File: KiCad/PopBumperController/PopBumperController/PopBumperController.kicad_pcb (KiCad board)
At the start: 2 copper layers, 132.5 x 83 mm, 63 parts, among them J1 Conn_01x02, J10 Conn_01x03, J11 Conn_01x03, J12 Conn_01x02, J13 Conn_01x03, J14 Conn_01x02, J15 Conn_01x03, J16 Conn_01x03, J2 Conn_01x03, J3 Conn_01x02, J4 Conn_01x02, J6 Conn_01x02, J7 Conn_01x02, J8 Conn_01x02, J9 Conn_01x03, Q1 TIP102, Q10 2N3904, Q11 TIP102, Q12 TIP102, Q13 2N3904, Q14 2N3904, Q16 TIP102, Q17 TIP102, Q2 TIP102, Q3 TIP102, Q4 2N3904, Q5 2N3904, Q6 2N3904, Q7 TIP102, Q8 TIP102, Q9 2N3904, U1 Pico

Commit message: Fix schematic issues, start PCB layout
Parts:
- removed the ? at (29.5, 115.5)
- removed the ? at (29.5, 42.5)
- removed J10, J11, J9: Conn_01x03, Connector_PinHeader_2.54mm:PinHeader_1x03_P2.54mm_Vertical
- removed J12, J14, J8, LED1, LED2, LED3, SOL1, SOL2, SOL3, SOL4, SOL5, SOL8, SOL9, SOL_L1, SOL_R1: Conn_01x02, Connector_JST:JST_XH_B2B-XH-A_1x02_P2.50mm_Vertical
- removed J13, J15, J16, SEN1, SEN2, SEN3, Vin1: Conn_01x03, Connector_JST:JST_XH_B3B-XH-A_1x03_P2.50mm_Vertical
- removed REF**: MountingHole_3.2mm_M3_ISO14580_Pad, MountingHole:MountingHole_3.2mm_M3_ISO14580_Pad
- added C1: 100 uF, Capacitor_THT:CP_Radial_D8.0mm_P3.50mm, F.Cu at (147.3, 152.4)
- added C10: 1000 uF, Capacitor_THT:CP_Radial_D10.0mm_P5.00mm, F.Cu at (268.3, 28.8)
- added C11: 100 uF, Capacitor_THT:CP_Radial_D8.0mm_P3.50mm, F.Cu at (323.0, 3.20)
- added C12: 15000 uF, Capacitor_THT:CP_Radial_D25.0mm_P10.00mm_SnapIn, F.Cu at (182.9, -18.3)
- added C2: 1000 uF, Capacitor_THT:CP_Radial_D10.0mm_P5.00mm, F.Cu at (300.0, 4.20)
- added C3: 1000 uF, Capacitor_THT:CP_Radial_D10.0mm_P5.00mm, F.Cu at (252.1, 54.1)
- added C4: 1000 uF, Capacitor_THT:CP_Radial_D10.0mm_P5.00mm, F.Cu at (253.0, 41.4)
- added C5: 1000 uF, Capacitor_THT:CP_Radial_D10.0mm_P5.00mm, F.Cu at (240.1, 61.9)
- added C6: 1000 uF, Capacitor_THT:CP_Radial_D10.0mm_P5.00mm, F.Cu at (282.2, 23.6)
- added C7: 1000 uF, Capacitor_THT:CP_Radial_D10.0mm_P5.00mm, F.Cu at (298.5, 15.8)
- added C8: 1000 uF, Capacitor_THT:CP_Radial_D10.0mm_P5.00mm, F.Cu at (286.7, 12.0)
- added C9: 1000 uF, Capacitor_THT:CP_Radial_D10.0mm_P5.00mm, F.Cu at (136.1, 43.2)
- added DT_SERVO1: 2.54mm, Connector_PinHeader_2.54mm:PinHeader_1x03_P2.54mm_Vertical, F.Cu at (106.7, 111.7)
- added DT_SERVO2: 2.54mm, Connector_PinHeader_2.54mm:PinHeader_1x03_P2.54mm_Vertical, F.Cu at (111.8, 111.7)
- added DT_SERVO3: 2.54mm, Connector_PinHeader_2.54mm:PinHeader_1x03_P2.54mm_Vertical, F.Cu at (116.8, 111.7)
- added DT_SW1: JST-XH x2, Connector_JST:JST_XH_B2B-XH-A_1x02_P2.50mm_Vertical, F.Cu at (110.5, 118.1)
- added DT_SW2: JST-XH x2, Connector_JST:JST_XH_B2B-XH-A_1x02_P2.50mm_Vertical, F.Cu at (110.5, 127.0)
- added DT_SW3: JST-XH x2, Connector_JST:JST_XH_B2B-XH-A_1x02_P2.50mm_Vertical, F.Cu at (110.5, 135.9)
- added J5: HYP_SIG, Connector_JST:JST_XH_B3B-XH-A_1x03_P2.50mm_Vertical, F.Cu at (105.5, 99.1)
- added L1: 47 mH, Inductor_THT:L_Radial_D12.0mm_P5.00mm_Fastron_11P, F.Cu at (135.9, 149.9)
- added LED_PB1: + -, Connector_JST:JST_XH_B2B-XH-A_1x02_P2.50mm_Vertical, F.Cu at (330.9, 11.3)
- added LED_PB2: + -, Connector_JST:JST_XH_B2B-XH-A_1x02_P2.50mm_Vertical, F.Cu at (292.8, 40.6)
- added LED_PB3: + -, Connector_JST:JST_XH_B2B-XH-A_1x02_P2.50mm_Vertical, F.Cu at (298.6, 32.7)
- added LED_SLL1: + -, Connector_JST:JST_XH_B2B-XH-A_1x02_P2.50mm_Vertical, F.Cu at (333.0, 1.80)
- added LED_SLR1: + -, Connector_JST:JST_XH_B2B-XH-A_1x02_P2.50mm_Vertical, F.Cu at (321.5, 11.3)
- added PB_SENS1: JST-XH x3, Connector_JST:JST_XH_B3B-XH-A_1x03_P2.50mm_Vertical, F.Cu at (288.0, 1.80)
- added PB_SENS2: JST-XH x3, Connector_JST:JST_XH_B3B-XH-A_1x03_P2.50mm_Vertical, F.Cu at (270.2, 18.6)
- added PB_SENS3: JST-XH x3, Connector_JST:JST_XH_B3B-XH-A_1x03_P2.50mm_Vertical, F.Cu at (240.1, 51.7)
- added Q15: 2N3904, Package_TO_SOT_THT:TO-92_Inline, F.Cu at (302.3, 48.2)
- added Q18: TIP102, Package_TO_SOT_THT:TO-220-3_Vertical, F.Cu at (311.5, 2.35)
- added Q19: 2N3904, Package_TO_SOT_THT:TO-92_Inline, F.Cu at (163.8, 31.8)
- added Q20: 2N3904, Package_TO_SOT_THT:TO-92_Inline, F.Cu at (306.6, 32.6)
- added Q21: TIP102, Package_TO_SOT_THT:TO-220-3_Vertical, F.Cu at (146.1, 33.2)
- added Q22: TIP102, Package_TO_SOT_THT:TO-220-3_Vertical, F.Cu at (293.7, 25.4)
- added R1: 330, Resistor_THT:R_Axial_DIN0309_L9.0mm_D3.2mm_P12.70mm_Horizontal, F.Cu at (240.5, 0.80)
- added R10: 470k, Resistor_THT:R_Axial_DIN0309_L9.0mm_D3.2mm_P12.70mm_Horizontal, F.Cu at (198.1, -16.5)
- added R11: 470k, Resistor_THT:R_Axial_DIN0309_L9.0mm_D3.2mm_P12.70mm_Horizontal, F.Cu at (147.3, 143.5)
- added R2: 330, Resistor_THT:R_Axial_DIN0309_L9.0mm_D3.2mm_P12.70mm_Horizontal, F.Cu at (224.6, 10.3)
- added R3: 330, Resistor_THT:R_Axial_DIN0309_L9.0mm_D3.2mm_P12.70mm_Horizontal, F.Cu at (240.5, 5.55)
- added R4: 330, Resistor_THT:R_Axial_DIN0309_L9.0mm_D3.2mm_P12.70mm_Horizontal, F.Cu at (224.6, 5.55)
- added R5: 330, Resistor_THT:R_Axial_DIN0309_L9.0mm_D3.2mm_P12.70mm_Horizontal, F.Cu at (224.6, 0.80)
- added R6: 330, Resistor_THT:R_Axial_DIN0309_L9.0mm_D3.2mm_P12.70mm_Horizontal, F.Cu at (224.6, 15.1)
- added R7: 330, Resistor_THT:R_Axial_DIN0309_L9.0mm_D3.2mm_P12.70mm_Horizontal, F.Cu at (256.3, 0.80)
- added R8: 330, Resistor_THT:R_Axial_DIN0309_L9.0mm_D3.2mm_P12.70mm_Horizontal, F.Cu at (158.8, 24.1)
- added R9: 330, Resistor_THT:R_Axial_DIN0309_L9.0mm_D3.2mm_P12.70mm_Horizontal, F.Cu at (224.6, 24.6)
- added SLING_L1: + - + -, Connector_JST:JST_XH_B4B-XH-A_1x04_P2.50mm_Vertical, F.Cu at (242.4, 11.3)
- added SLING_R1: + - + -, Connector_JST:JST_XH_B4B-XH-A_1x04_P2.50mm_Vertical, F.Cu at (258.2, 6.55)
- added SOL_DRAIN1: + -, Connector_JST:JST_XH_B2B-XH-A_1x02_P2.50mm_Vertical, F.Cu at (170.2, 39.4)
- added SOL_FLIP_L1: + -, Connector_JST:JST_XH_B2B-XH-A_1x02_P2.50mm_Vertical, F.Cu at (284.8, 50.6)
- added SOL_FLIP_R1: + -, Connector_JST:JST_XH_B2B-XH-A_1x02_P2.50mm_Vertical, F.Cu at (277.5, 58.4)
- added SOL_HYP1: + -, Connector_JST:JST_XH_B2B-XH-A_1x02_P2.50mm_Vertical, F.Cu at (277.5, 66.2)
- added SOL_PB1: + -, Connector_JST:JST_XH_B2B-XH-A_1x02_P2.50mm_Vertical, F.Cu at (275.4, 50.6)
- added SOL_PB2: + -, Connector_JST:JST_XH_B2B-XH-A_1x02_P2.50mm_Vertical, F.Cu at (342.5, 1.80)
- added SOL_PB3: + -, Connector_JST:JST_XH_B2B-XH-A_1x02_P2.50mm_Vertical, F.Cu at (268.1, 62.4)
- added SOL_SLING_L1: + -, Connector_JST:JST_XH_B2B-XH-A_1x02_P2.50mm_Vertical, F.Cu at (324.4, 19.1)
- added SOL_SLING_R1: + -, Connector_JST:JST_XH_B2B-XH-A_1x02_P2.50mm_Vertical, F.Cu at (305.5, 24.9)
- BTNL1, BTNR1: value Conn_01x04 -> JST-XH x4
- J1: value Conn_01x02 -> UNUSED
- J2: value Conn_01x03 -> POWER
- J3: value Conn_01x02 -> UART; footprint Connector_JST:JST_XH_B4B-XH-A_1x04_P2.50mm_Vertical -> Connector_JST:JST_XH_B3B-XH-A_1x03_P2.50mm_Vertical
- J4: value Conn_01x02 -> DRAIN_SIG; footprint Connector_JST:JST_XH_B4B-XH-A_1x04_P2.50mm_Vertical -> Connector_JST:JST_XH_B3B-XH-A_1x03_P2.50mm_Vertical
- J6: value Conn_01x02 -> HYP_SIG2
- J7: value Conn_01x02 -> DRAIN_SIG2
- Q1, Q11, Q12, Q16, Q2, Q3: value TIP102 -> 2N3904; footprint Package_TO_SOT_THT:TO-220-3_Vertical -> Package_TO_SOT_THT:TO-92_Inline
- Q10, Q14, Q4: value 2N3904 -> TIP102; footprint Package_TO_SOT_THT:TO-92_Inline -> Package_TO_SOT_THT:TO-220-3_Vertical
- moved Q16 277.3 mm to (322.9, 26.8), turned to 0 degrees
- moved D5 246.4 mm to (272.5, 0.55)
- moved Q5 244.9 mm to (345.4, 9.48), turned to 0 degrees
- moved Q6 235.0 mm to (338.9, 15.3), turned to 0 degrees
- moved Q13 234.2 mm to (332.4, 19.0), turned to 0 degrees
- moved Q17 226.0 mm to (276.3, 39.2), turned to 0 degrees
- moved D4 222.7 mm to (254.7, 17.9)
- moved Q3 215.1 mm to (338.9, 9.48), turned to 0 degrees
- moved Q9 212.6 mm to (285.5, 58.3), turned to 0 degrees
- moved Q11 208.5 mm to (310.2, 40.4), turned to 0 degrees
- moved Q7 208.2 mm to (263.6, 57.0), turned to 0 degrees
- moved D9 206.4 mm to (239.4, 30.6), turned to 0 degrees
- moved Q12 203.7 mm to (292.8, 56.0), turned to 0 degrees
- moved Q1 198.3 mm to (319.6, 34.6), turned to 0 degrees
- moved Q8 196.4 mm to (251.7, 63.8), turned to 0 degrees
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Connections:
- BTNL1 pad 1: /LED_L -> Net-(BTNL1-Pad1)
- BTNL1 pad 2: /5V -> +5V
- BTNL1 pad 4: /3V3 -> +3V3
- BTNR1 pad 1: /LED_R -> Net-(BTNR1-Pad1)
- BTNR1 pad 2: /5V -> +5V
- BTNR1 pad 4: /3V3 -> +3V3
- D1 pad 1: /12V -> +12V
- D1 pad 2: /SOL1 -> Net-(SOL_PB1-Pad2)
- D2 pad 1: /12V -> +12V
- D2 pad 2: /SOL2 -> Net-(D2-Pad2)
- D3 pad 1: /12V -> +12V
- D3 pad 2: /SOL3 -> Net-(D3-Pad2)
- D4 pad 1: /12V -> +12V
- D4 pad 2: /SOL4 -> Net-(D4-Pad2)
- D5 pad 1: /12V -> +12V
- D5 pad 2: /SOL5 -> Net-(D5-Pad2)
- D6 pad 1: /12V -> +12V
- D6 pad 2: /SOL6 -> Net-(D6-Pad2)
- D7 pad 1: /12V -> +12V
- D7 pad 2: /SOL7 -> Net-(D7-Pad2)
- D8 pad 1: /12V -> +12V
- D8 pad 2: /SOL8 -> Net-(D8-Pad2)
- D9 pad 1: /12V -> +12V
- D9 pad 2: /SOL9 -> Net-(D9-Pad2)
- J1 pad 1: /GND -> GND
- J1 pad 2: /UART_TX -> Net-(U1-Pad20)
- J1 pad 3: /UART_RX -> Net-(U1-Pad19)
- J2 pad 1: /SOL1_en -> GND
- J2 pad 2: /SOL2_En -> +5V
- J2 pad 3: /SOL3_en -> +12V
- J3 pad 1: /3V3 -> GND
- J3 pad 2: /Sling_L_Switch -> /UART_TX
- J3 pad 3: /3V3 -> /UART_RX
- J4 pad 1: /3V3 -> +5V
- J4 pad 2: /Sling_R_Switch -> GND
- J4 pad 3: /3V3 -> /DRAIN_SIGNAL
- J6 pad 1: /GND -> +5V
- J6 pad 2: /DRP1 -> GND
- J7 pad 1: /GND -> +5V
- J7 pad 2: /DRP2 -> GND
- Q1 pad 1: /SOL1_en -> /Sling_L_Switch_triggered
- Q1 pad 2: /SOL1 -> Net-(SLING_L1-Pad4)
- Q1 pad 3: /GND -> +3V3
- Q10 pad 1: /Sling_R_Switch_triggered -> Net-(Q10-Pad1)
- Q10 pad 2: /Sling_R_Switch -> Net-(D4-Pad2)
- Q10 pad 3: /3V3 -> GND
- Q11 pad 1: /SOL_L_EN -> GND
- Q11 pad 2: /SOL6 -> /TRIGGER_L
- Q11 pad 3: /GND -> Net-(BTNL1-Pad1)
- Q12 pad 1: /SOL_R_EN -> GND
- Q12 pad 2: /SOL7 -> /TRIGGER_R
- Q12 pad 3: /GND -> Net-(BTNR1-Pad1)
- Q13 pad 1: /GND -> Net-(Q13-Pad1)
- Q13 pad 2: /TRIGGER_L -> Net-(Q13-Pad2)
- Q13 pad 3: /LED_L -> +5V
- Q14 pad 1: /GND -> Net-(Q13-Pad1)
- Q14 pad 2: /TRIGGER_R -> Net-(D5-Pad2)
- Q14 pad 3: /LED_R -> GND
- Q16 pad 1: /SOL_RELOAD_EN -> Net-(Q16-Pad1)
- Q16 pad 2: /SOL8 -> Net-(Q16-Pad2)
- Q16 pad 3: /GND -> Net-(LED_PB3-Pad2)
- Q17 pad 1: /SOL_HYP_EN -> Net-(Q15-Pad1)
- Q17 pad 2: /SOL9 -> Net-(D6-Pad2)
- Q17 pad 3: /GND -> GND
- Q2 pad 1: /SOL2_En -> /Sling_R_Switch_triggered
- Q2 pad 2: /SOL2 -> Net-(SLING_R1-Pad2)
- Q2 pad 3: /GND -> +3V3
- Q3 pad 1: /SOL3_en -> Net-(Q3-Pad1)
- Q3 pad 2: /SOL3 -> Net-(Q3-Pad2)
- Q3 pad 3: /GND -> Net-(LED_PB1-Pad2)
- Q4 pad 1: /GND -> Net-(Q3-Pad1)
- Q4 pad 2: /SOL1_en -> Net-(SOL_PB1-Pad2)
- Q4 pad 3: /LED1 -> GND
- Q5 pad 1: /GND -> Net-(Q5-Pad1)
- Q5 pad 2: /SOL2_En -> Net-(Q5-Pad2)
- Q5 pad 3: /LED2 -> Net-(LED_SLL1-Pad2)
- Q6 pad 1: /GND -> Net-(Q6-Pad1)
- Q6 pad 2: /SOL3_en -> Net-(Q6-Pad2)
- Q6 pad 3: /LED3 -> Net-(LED_SLR1-Pad2)
- Q7 pad 1: /Sling_L_en -> Net-(Q5-Pad1)
- Q7 pad 2: /SOL4 -> Net-(D2-Pad2)
- Q7 pad 3: /GND -> GND
- Q8 pad 1: /Sling_R_en -> Net-(Q6-Pad1)
- Q8 pad 2: /SOL5 -> Net-(D3-Pad2)
- Q8 pad 3: /GND -> GND
- Q9 pad 1: /Sling_L_Switch_triggered -> Net-(Q10-Pad1)
- Q9 pad 2: /Sling_L_Switch -> Net-(Q9-Pad2)
- Q9 pad 3: /3V3 -> Net-(LED_PB2-Pad2)
- U1 pad 13: /GND -> GND
- U1 pad 18: /GND -> GND
- U1 pad 21: /SOL_R_EN -> /FLIPPER_R
- U1 pad 22: /SOL_L_EN -> /FLIPPER_L
- U1 pad 23: /GND -> GND
- U1 pad 26: /SOL1_en -> /POP_BUMPER1
- U1 pad 27: /SOL2_En -> /POP_BUMPER2
- U1 pad 28: /GND -> GND
- U1 pad 29: /SOL3_en -> /POP_BUMPER3
- U1 pad 3: /GND -> GND
- U1 pad 31: /Sensor1 -> /PB_SENSOR1
- U1 pad 32: /Sensor2 -> /PB_SENSOR2
- U1 pad 33: /GND -> GND
- U1 pad 34: /Sensor3 -> /PB_SENSOR3
- U1 pad 36: /3V3 -> +3V3
- U1 pad 38: /GND -> GND
- U1 pad 4: /Sling_L_en -> /SLING_L
- U1 pad 40: /5V -> +5V
- U1 pad 42: /GND -> unconnected-(U1-Pad42)
- U1 pad 5: /Sling_R_en -> /SLING_R
- U1 pad 8: /GND -> GND
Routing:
- net /12V: track 340.3 -> 0.00 mm
- net /3V3: track 276.3 -> 0.00 mm
- net /5V: track 118.6 -> 0.00 mm, vias 1 -> 0
- net /SOL3_en: track 91.3 -> 0.00 mm
- net /SOL2_En: track 63.8 -> 0.00 mm
- net /DRP_Servo: track 55.5 -> 0.00 mm
- net /UART_TX: track 49.3 -> 0.00 mm
- net /Sling_L_en: track 49.0 -> 0.00 mm
- net /SOL7: track 47.5 -> 0.00 mm
- net /SOL1_en: track 46.6 -> 0.00 mm
- net /UART_RX: track 45.2 -> 0.00 mm
- net /TRIGGER_R: track 43.8 -> 0.00 mm
- net /SOL6: track 40.8 -> 0.00 mm
- net /Sling_R_en: track 35.1 -> 0.00 mm
- net /DRP1: track 34.2 -> 0.00 mm
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- removed copper zone on B.Cu, net /GND
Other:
- board outline removed
- board text added: "5V GND"
- board text added: "5V GND SIG"
- board text added: "GND 5V SER"
- board text added: "GND GP15 GP14"
- board text added: "RX TX GND"
- board text removed: "+ -"
- board text removed: "+ - SIG"
- board text removed: "+ DRAIN -"
- board text removed: "+ HYP -"
- board text removed: "+ IR_DR_E -"
- board text removed: "+ SOL_L -"
- board text removed: "+ SOL_R -"
- board text removed: "- +"
- board text removed: "- + SW_L - +"
- board text removed: "- + SW_R - +"
- board text removed: "- FLIP_L +"
- board text removed: "- FLIP_R +"
- board text removed: "1 2 3"
- board text removed: "12V"
- board text removed: "14"
- board text removed: "15"
- board text removed: "3V3"
- board text removed: "5V"
- board text removed: "B+"
- board text removed: "B-"
- board text removed: "DRAIN"
- board text removed: "DROP TARGETS"
- board text removed: "DT_SERVO"
- board text removed: "DT_SW1"
- board text removed: "DT_SW2"
- board text removed: "DT_SW3"
- board text removed: "Designed by Mark Hutcheson Feb 2022"
- board text removed: "FLIPPERS"
- board text removed: "GND"
- board text removed: "HYPERSPACE"
- board text removed: "IR_DR_S"
- board text removed: "IR_HYP_E"
- board text removed: "IR_HYP_S"
- board text removed: "LED+"
- board text removed: "LED-"
- board text removed: "OUT"
- board text removed: "POP BUMPERS"
- board text removed: "PWM"
- board text removed: "RX"
- board text removed: "SLINGSHOTS"
- board text removed: "SOL_EN"
- board text removed: "TX"
- board text removed: "UART"
- board text removed: "UNUSED"

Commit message: placement
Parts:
- added ? (x2): , , F.Cu at (54.6, 142.2)
- added ? (x2): , , F.Cu at (241.3, 142.2)
- added ? (x2): , , F.Cu at (241.3, 55.9)
- J3: footprint Connector_JST:JST_XH_B3B-XH-A_1x03_P2.50mm_Vertical -> Connector_JST:JST_XH_B2B-XH-A_1x02_P2.50mm_Vertical
- moved Q5 277.9 mm to (72.4, 61.2)
- moved Q6 273.2 mm to (73.8, 81.5)
- moved SOL_SLING_L1 264.5 mm to (64.3, 67.1)
- moved Q20 264.4 mm to (63.7, 137.2)
- moved LED_SLL1 260.8 mm to (82.5, 73.9), turned to 90 degrees
- moved Q22 258.2 mm to (58.6, 132.3), turned to 90 degrees
- moved LED_SLR1 249.9 mm to (82.5, 84.1), turned to 90 degrees
- moved SOL_SLING_R1 249.3 mm to (64.2, 87.4)
- moved SOL_HYP1 222.8 mm to (63.7, 128.8)
- moved C10 220.5 mm to (67.4, 119.6), turned to 180 degrees
- moved Q2 212.8 mm to (101.6, 58.4), turned to 90 degrees
- moved Q7 205.2 mm to (58.9, 70.1), turned to 90 degrees
- moved Q1 199.1 mm to (121.9, 58.4), turned to 90 degrees
- moved Q8 194.7 mm to (58.8, 90.4), turned to 90 degrees
- moved D9 192.6 mm to (71.3, 124.7), turned to -90 degrees
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- renumbered BTNL1 to BTNL, BTNR1 to BTNR, SOL_FLIP_L1 to SOL_FLIP_L
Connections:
- J3 pad 1: GND -> /UART_TX
- J3 pad 2: /UART_TX -> /UART_RX
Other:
- board outline added: 196.8 x 96.5 mm
- board text added: "GND 5V 12V"
- board text added: "L- L+ B- B+"
- board text added: "RX TX"
- board text added: "S GND 3V"
- board text removed: "RX TX GND"

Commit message: yay dun wiren
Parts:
- removed the ? at (54.6, 142.2)
- removed the ? at (241.3, 55.9)
- removed the ? at (241.3, 142.2)
- moved J2 21.6 mm to (110.5, 139.9)
- moved C12 9.67 mm to (157.5, 138.0)
- moved R10 8.98 mm to (142.2, 139.7)
- moved Q2 3.30 mm to (102.8, 61.5)
- moved SLING_R1 3.30 mm to (88.9, 59.7)
- moved Q1 3.30 mm to (123.1, 61.5)
- moved SLING_L1 3.30 mm to (109.2, 59.7)
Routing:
- net +5V: track 0.00 -> 319.0 mm, vias 0 -> 2
- net +3V3: track 0.00 -> 176.3 mm
- net /SLING_L: track 0.00 -> 158.1 mm, vias 0 -> 2
- net /SLING_R: track 0.00 -> 136.6 mm, vias 0 -> 2
- net /POP_BUMPER3: track 0.00 -> 130.6 mm, vias 0 -> 1
- net /FLIPPER_L: track 0.00 -> 127.2 mm, vias 0 -> 2
- net /SOL_RELOAD_EN: track 0.00 -> 111.1 mm, vias 0 -> 2
- net /FLIPPER_R: track 0.00 -> 110.8 mm, vias 0 -> 3
- net /POP_BUMPER2: track 0.00 -> 108.9 mm, vias 0 -> 1
- net /HYP_SIGNAL: track 0.00 -> 97.2 mm
- net /POP_BUMPER1: track 0.00 -> 88.8 mm, vias 0 -> 1
- net /SOL_HYP_EN: track 0.00 -> 84.2 mm, vias 0 -> 2
- net /DRAIN_SIGNAL: track 0.00 -> 64.4 mm
- net /TRIGGER_L: track 0.00 -> 54.0 mm, vias 0 -> 2
- net /DRP3: track 0.00 -> 41.3 mm
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- added copper zone on F.Cu, net +12V
- added copper zone on F.Cu, net +5V
- added copper zone on B.Cu, net GND
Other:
- outline, holes or cut-outs redrawn

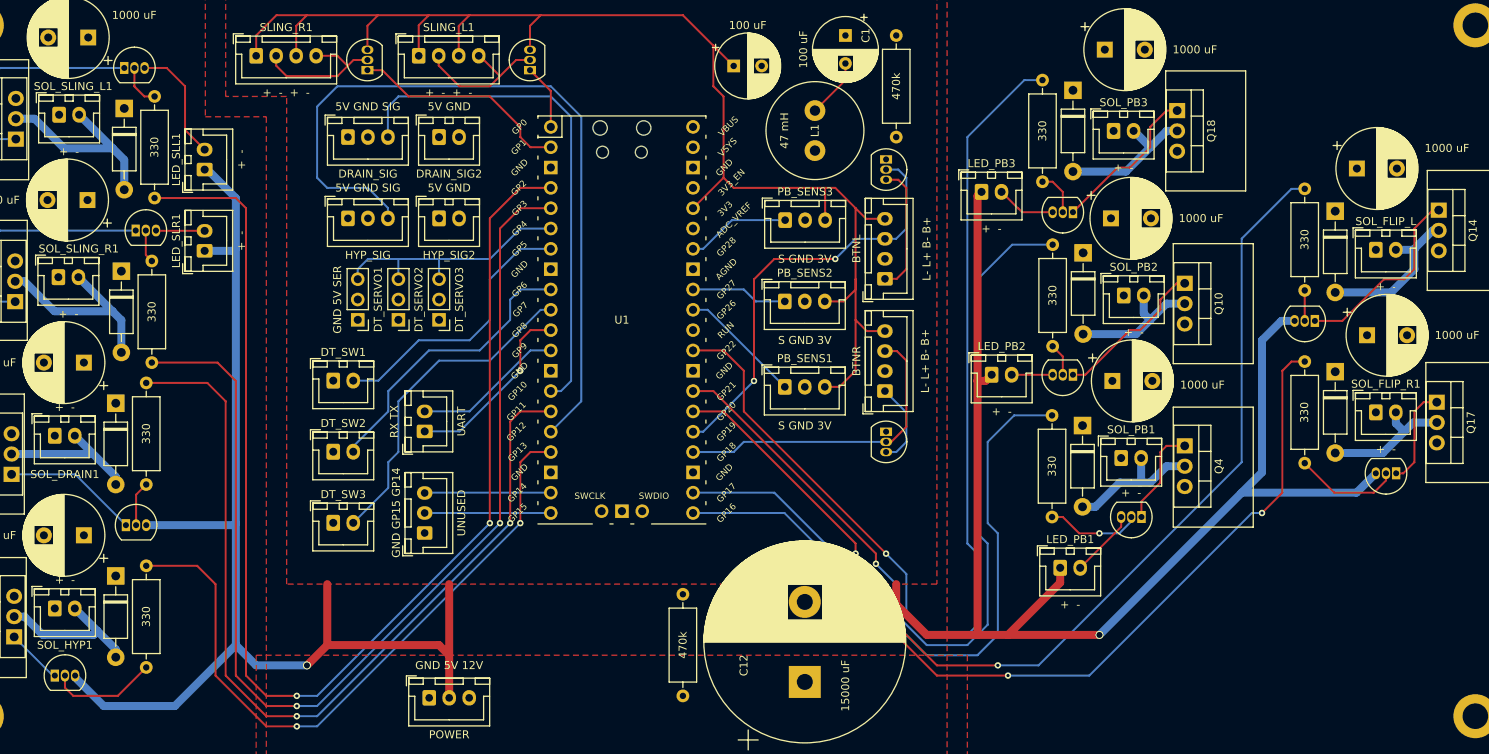
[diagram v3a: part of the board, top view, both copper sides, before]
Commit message: Bracket assembly updates, new solenoid controller pcb design, new driver to potentially use a different display
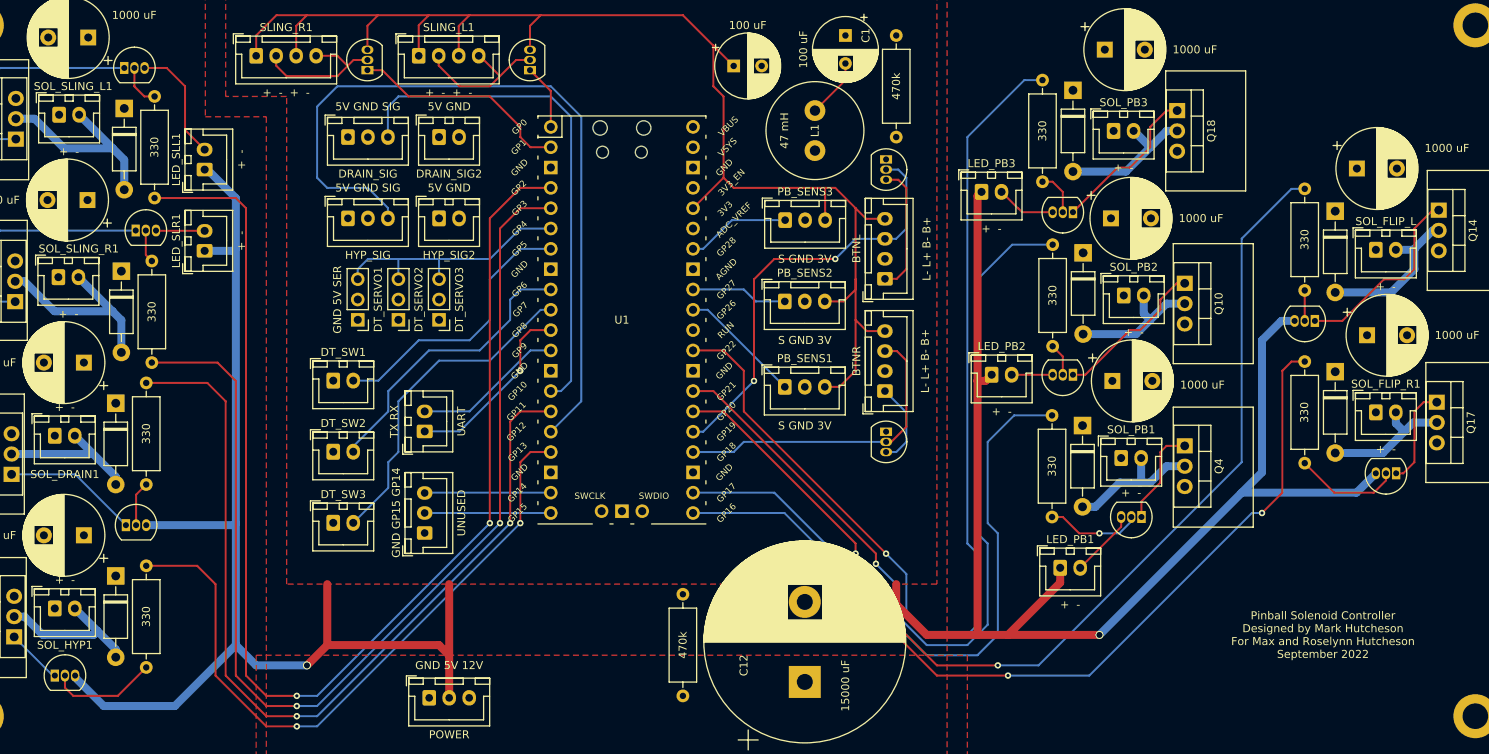
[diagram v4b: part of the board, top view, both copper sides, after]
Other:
- board text added: "Pinball Solenoid Controller Designed by Mark Hutcheson For Max and Roselynn Hutcheson September 2022"
- board text added: "TX RX"
- board text removed: "RX TX"
